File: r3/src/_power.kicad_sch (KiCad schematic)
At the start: 51 parts, among them J10 Conn_01x05_MountingPin, Q1 Si7113ADN, Q2 Si7113ADN, Q3 Si7113ADN, U2 ESD7004, U3 DZDH0401DW, U4 DZDH0401DW, U5 LM60440DRPK, U6 LM60440DRPK

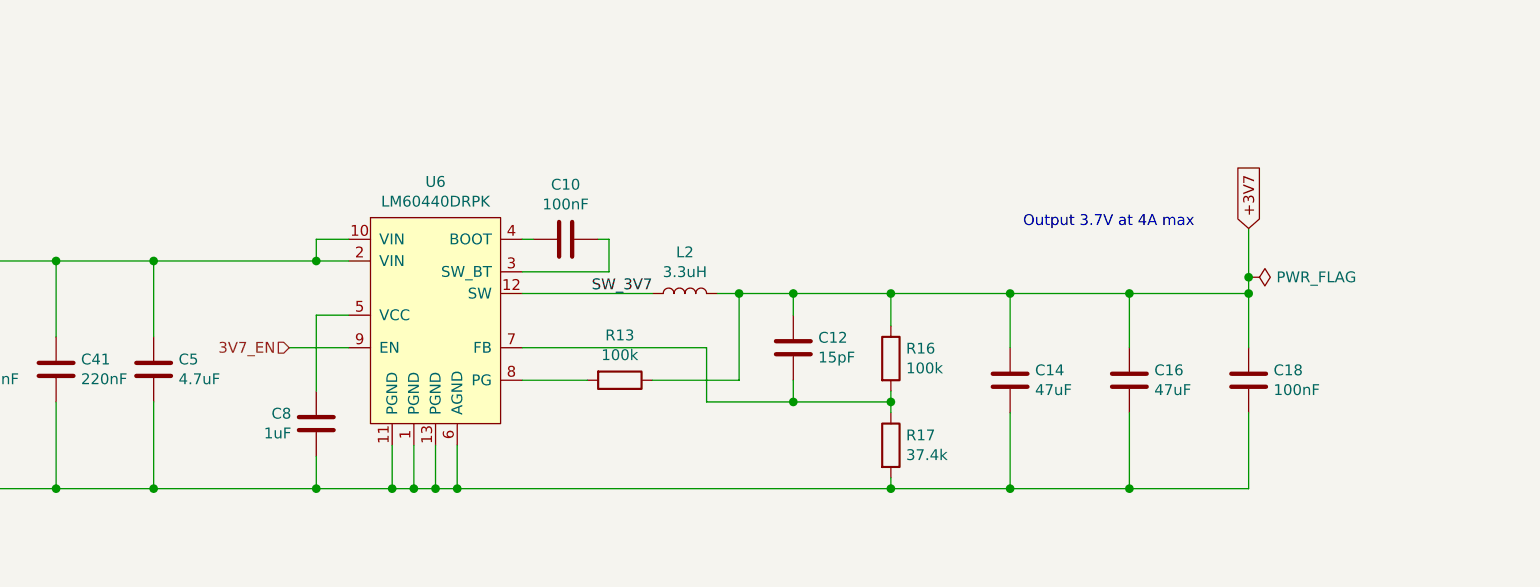
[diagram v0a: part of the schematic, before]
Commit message: Add pull-down on 3V7_EN
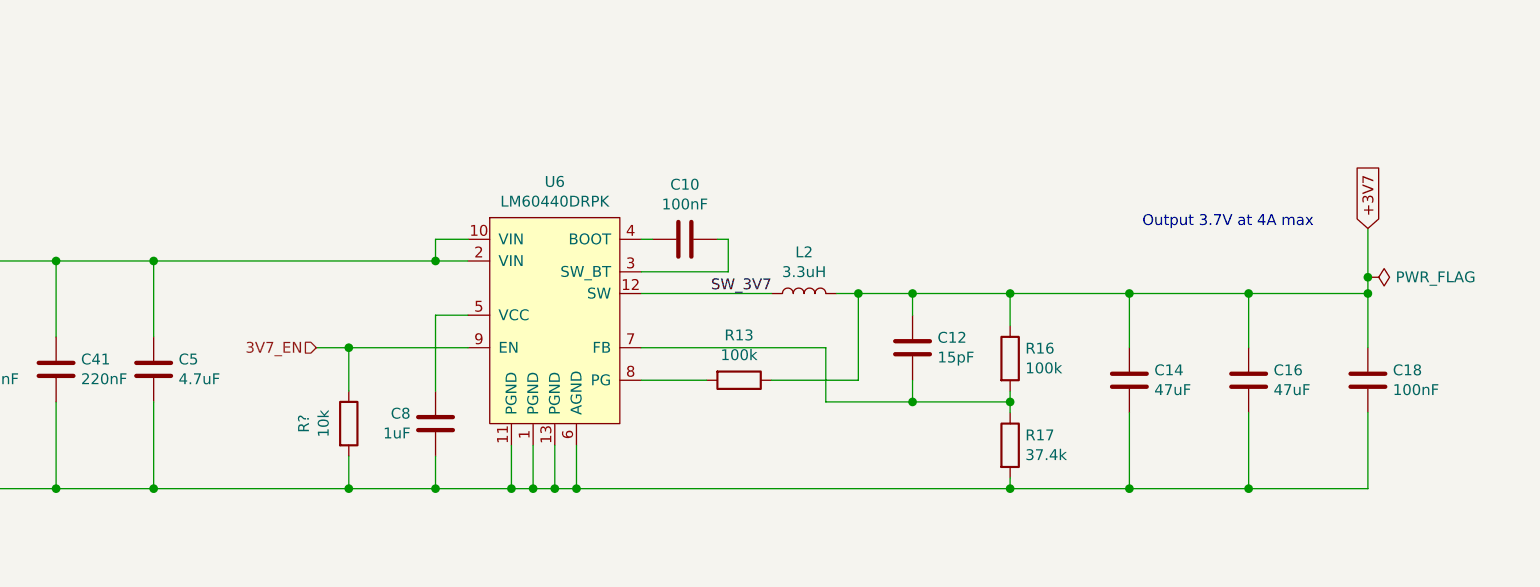
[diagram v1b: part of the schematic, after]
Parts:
- added R?: 10k, Resistor_SMD:R_0603_1608Metric, symbol Device:R
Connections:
- net 3V7_EN: now also R?.1
- net GND: now also R?.2
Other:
- moved on the sheet: C10, C12, C14, C16, C18, C8, L2, R13, R16, R17, U6

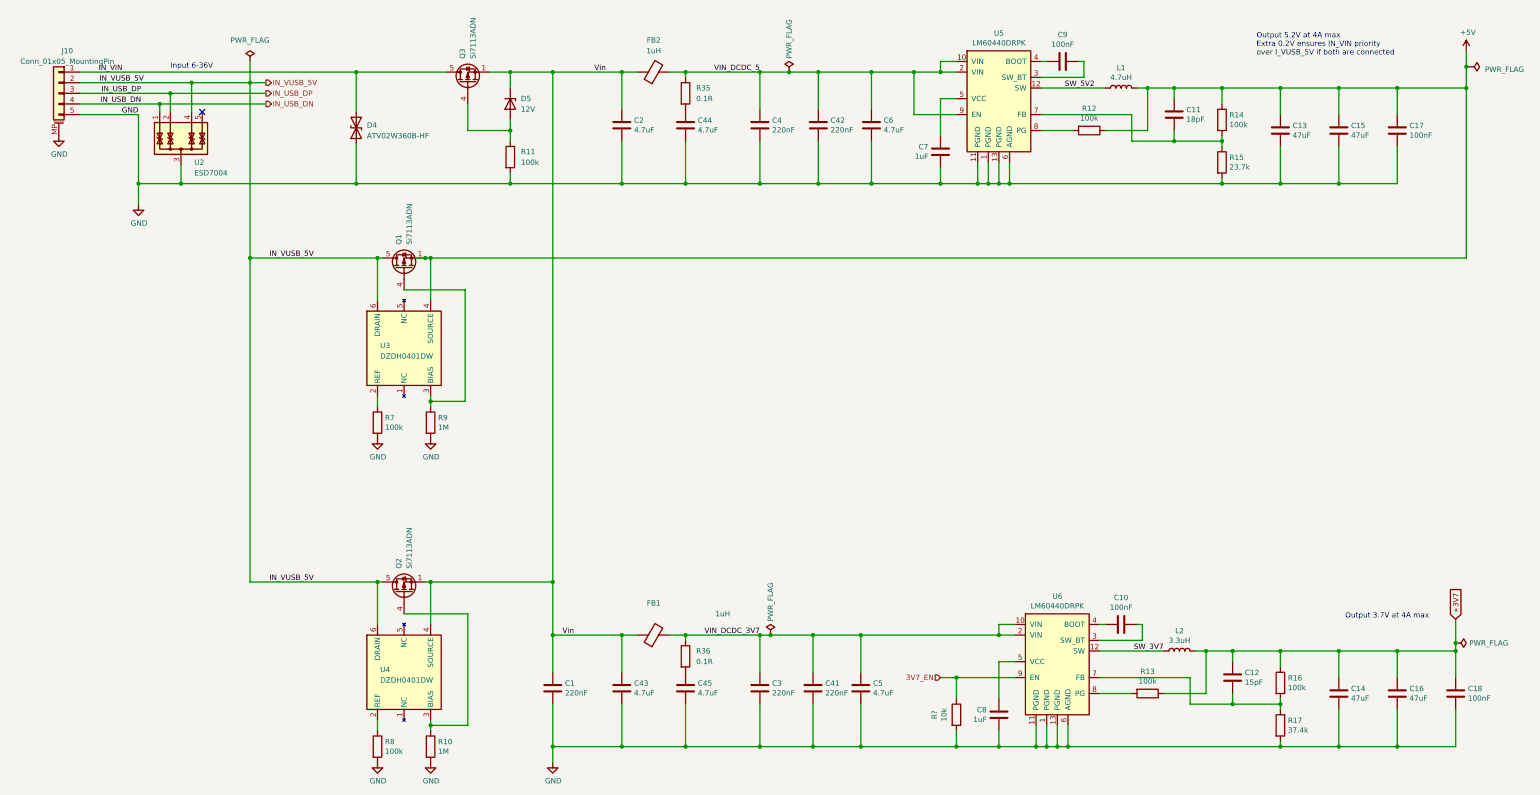
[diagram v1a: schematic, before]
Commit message: Change to Molex CLIK-Mate for input connector
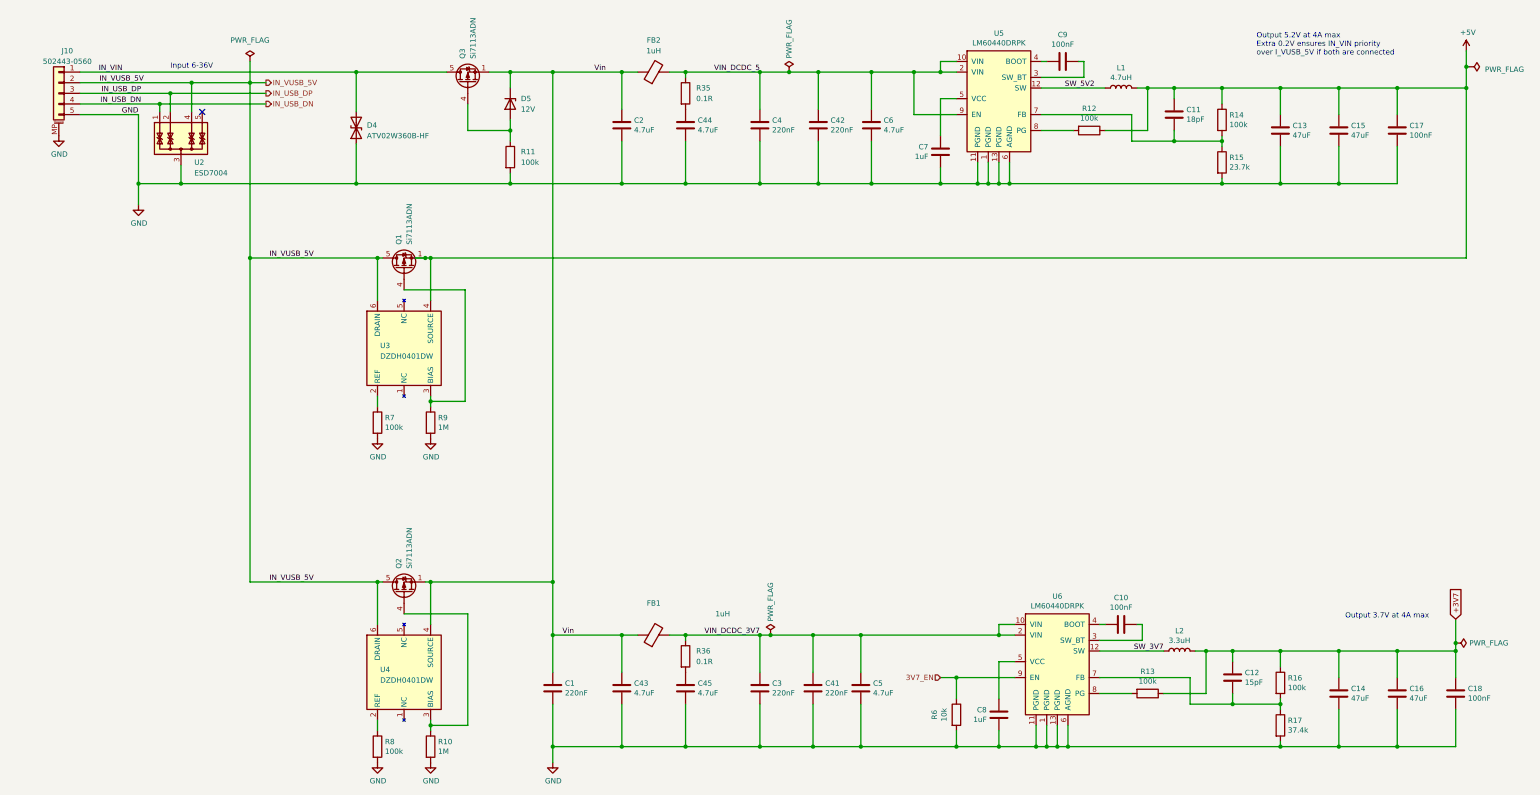
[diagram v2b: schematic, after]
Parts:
- J10: value Conn_01x05_MountingPin -> 502443-0560; footprint Connector_JST:JST_PH_B5B-PH-SM4-TB_1x05-1MP_P2.00mm_Vertical -> Connector_Molex:Molex_CLIK-Mate_502443-0570_1x05-1MP_P2.00mm_Vertical
- gave numbers to parts that had none: 1
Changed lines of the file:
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@@
   (symbol (lib_id "Device:R") (at 264.16 220.98 0) (unit 1)
     (in_bom yes) (on_board yes)
-    (property "Reference" "R?" (id 0) (at 258.9022 220.98 90))
+    (property "Reference" "R6" (id 0) (at 258.9022 220.98 90))
     (property "Value" "10k" (id 1) (at 261.2136 220.98 90))
     (property "Footprint" "Resistor_SMD:R_0603_1608Metric" (id 2) (at 262.382 220.98 90)
@@
     (in_bom yes) (on_board yes)
     (property "Reference" "J10" (id 0) (at 51.562 62.23 0))
-    (property "Value" "Conn_01x05_MountingPin" (id 1) (at 51.562 64.77 0))
-    (property "Footprint" "Connector_JST:JST_PH_B5B-PH-SM4-TB_1x05-1MP_P2.00mm_Vertical" (id 2) (at 49.53 72.39 0)
-      (effects (font (size 1.27 1.27)) hide)
-    )
+    (property "Value" "502443-0560" (id 1) (at 51.562 64.77 0))
+    (property "Footprint" "Connector_Molex:Molex_CLIK-Mate_502443-0570_1x05-1MP_P2.00mm_Vertical" (id 2) (at 49.53 72.39 0)
+      (effects (font (size 1.27 1.27)) hide)
+    )

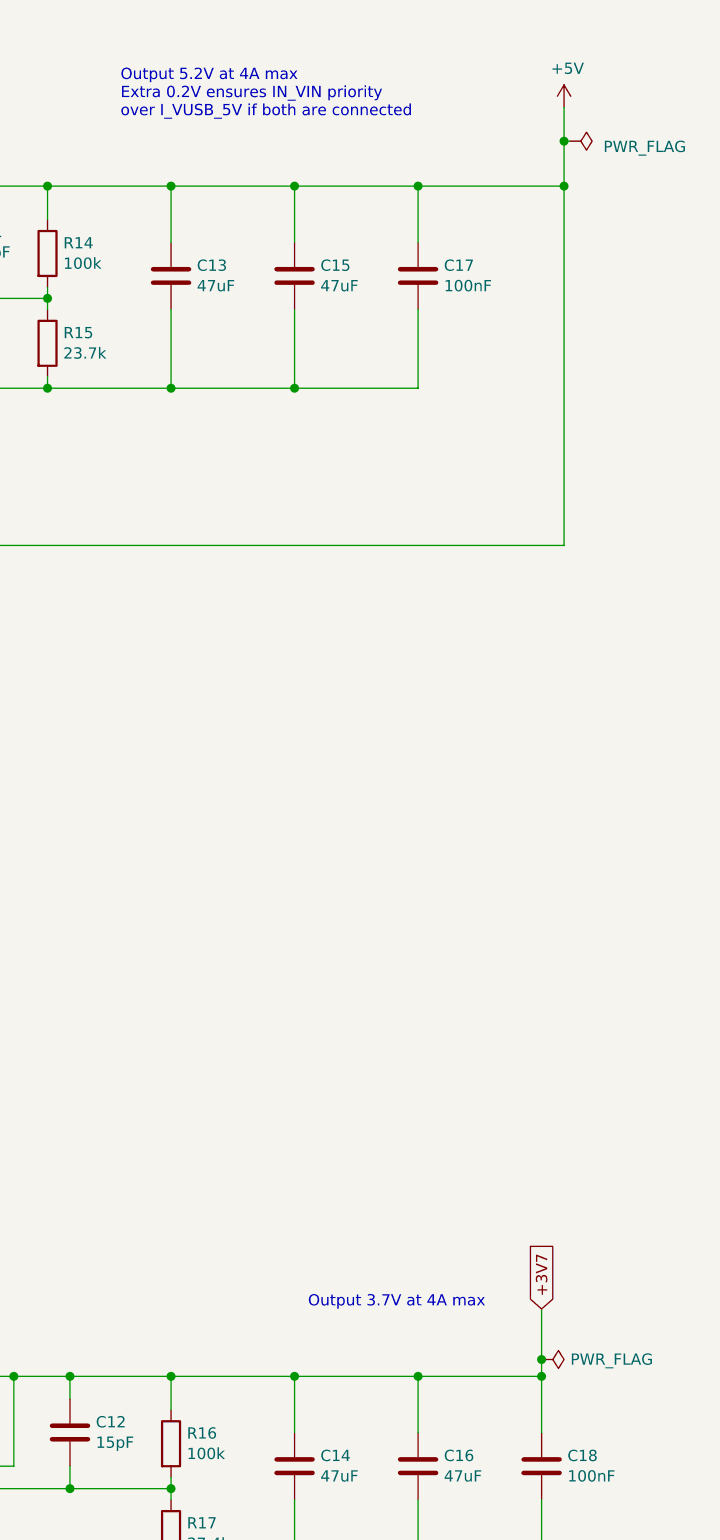
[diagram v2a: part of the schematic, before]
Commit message: Add 5V and 3V7 test points
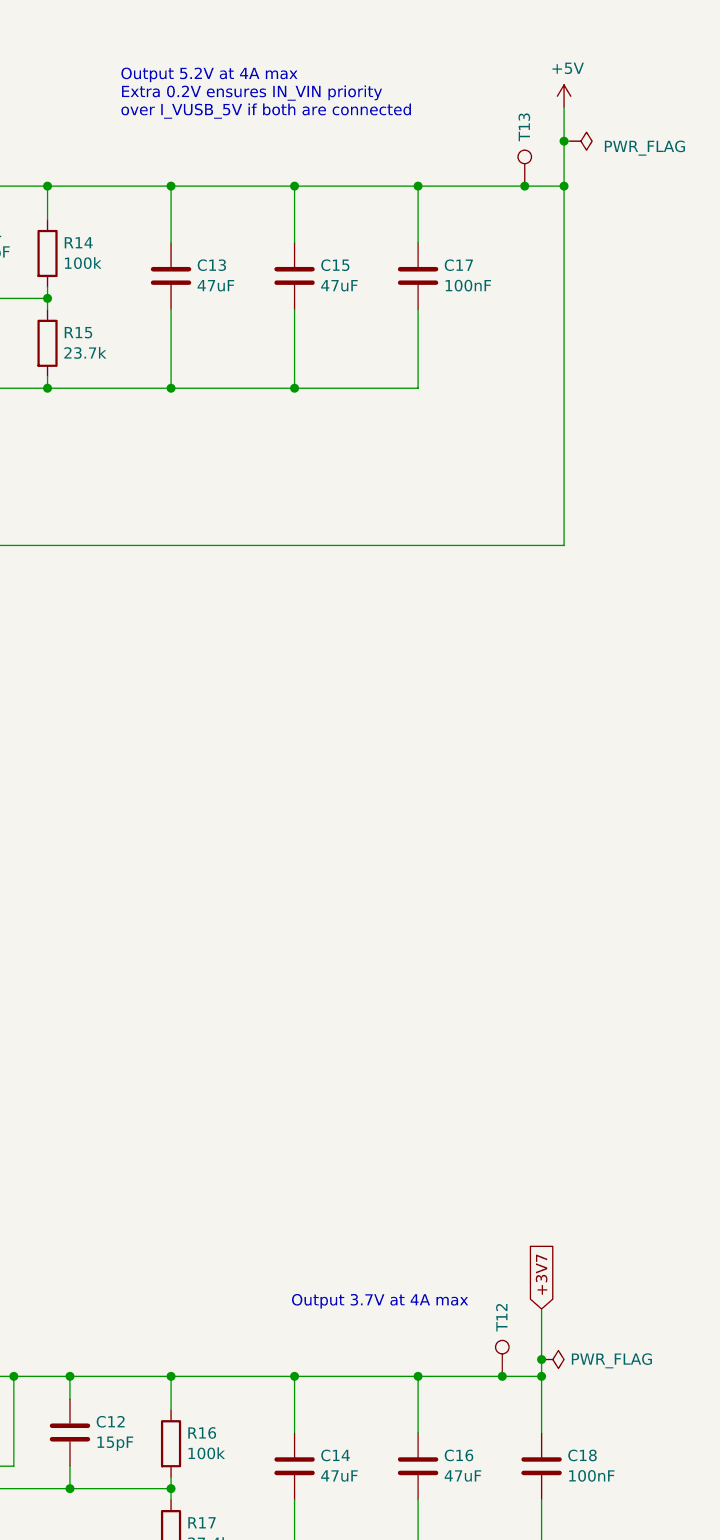
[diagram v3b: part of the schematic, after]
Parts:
- added T12, T13: (no value), TestPoint:TestPoint_Pad_D1.0mm, symbol Connector:TestPoint
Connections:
- net +3V7: now also T12.1
- net +5V: now also T13.1
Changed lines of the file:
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@@
   (junction (at 369.57 205.74) (diameter 1.016) (color 0 0 0 0))
   (junction (at 369.57 228.6) (diameter 1.016) (color 0 0 0 0))
+  (junction (at 379.095 205.74) (diameter 1.016) (color 0 0 0 0))
+  (junction (at 381.635 71.12) (diameter 1.016) (color 0 0 0 0))
   (junction (at 383.54 203.835) (diameter 1.016) (color 0 0 0 0))
   (junction (at 383.54 205.74) (diameter 1.016) (color 0 0 0 0))
@@
     (stroke (width 0) (type solid) (color 0 0 0 0))
   )
-  (wire (pts (xy 369.57 71.12) (xy 386.08 71.12))
+  (wire (pts (xy 369.57 71.12) (xy 381.635 71.12))
     (stroke (width 0) (type solid) (color 0 0 0 0))
   )
@@
     (stroke (width 0) (type solid) (color 0 0 0 0))
   )
-  (wire (pts (xy 369.57 205.74) (xy 383.54 205.74))
+  (wire (pts (xy 369.57 205.74) (xy 379.095 205.74))
     (stroke (width 0) (type solid) (color 0 0 0 0))
   )
   (wire (pts (xy 369.57 219.71) (xy 369.57 228.6))
+    (stroke (width 0) (type solid) (color 0 0 0 0))
+  )
+  (wire (pts (xy 379.095 205.74) (xy 383.54 205.74))
+    (stroke (width 0) (type solid) (color 0 0 0 0))
+  )
+  (wire (pts (xy 381.635 71.12) (xy 386.08 71.12))
     (stroke (width 0) (type solid) (color 0 0 0 0))
   )
@@
     (effects (font (size 1.27 1.27)) (justify left bottom))
   )
-  (text "Output 3.7V at 4A max" (at 377.19 198.12 180)
+  (text "Output 3.7V at 4A max" (at 375.285 198.12 180)
     (effects (font (size 1.27 1.27)) (justify right bottom))
   )
@@
       (effects (font (size 1.27 1.27)) hide)
     )
+    (pin "1")
+  )
+  (symbol (lib_id "Connector:TestPoint") (at 379.095 205.74 0) (unit 1)
+    (in_bom yes) (on_board yes)
+    (property "Reference" "T12" (id 0) (at 379.095 200.66 90)
+      (effects (font (size 1.27 1.27)) (justify left))
+    )
+    (property "Value" " " (id 1) (at 377.825 200.66 90)
+      (effects (font (size 1.27 1.27)) (justify left))
+    )
+    (property "Footprint" "TestPoint:TestPoint_Pad_D1.0mm" (id 2) (at 384.175 205.74 0)
+      (effects (font (size 1.27 1.27)) hide)
+    )
+    (property "Datasheet" "~" (id 3) (at 384.175 205.74 0)
+      (effects (font (size 1.27 1.27)) hide)
+    )
+    (pin "1")
+  )
+  (symbol (lib_id "Connector:TestPoint") (at 381.635 71.12 0) (unit 1)
+    (in_bom yes) (on_board yes)
+    (property "Reference" "T13" (id 0) (at 381.635 66.04 90)
+      (effects (font (size 1.27 1.27)) (justify left))
+    )
+    (property "Value" " " (id 1) (at 380.365 66.04 90)
+      (effects (font (size 1.27 1.27)) (justify left))
+    )
+    (property "Footprint" "TestPoint:TestPoint_Pad_D1.0mm" (id 2) (at 386.715 71.12 0)
+      (effects (font (size 1.27 1.27)) hide)
+    )
+    (property "Datasheet" "~" (id 3) (at 386.715 71.12 0)
+      (effects (font (size 1.27 1.27)) hide)
+    )

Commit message: Change to new 5-pin variant of the protection diode network symbol
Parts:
- U2: footprint jeffmakes-footprints:USON-10_2.5x1.0mm_P0.5mm -> Package_SON:USON-10_2.5x1.0mm_P0.5mm; symbol Power_Protection:TPD4E02B04DQA -> j_Power_Protection:ESD7004
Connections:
- net GND: no longer U2.8 (G)
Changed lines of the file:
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@@
     (pin "MP")
   )
-  (symbol (lib_id "Power_Protection:TPD4E02B04DQA") (at 78.74 84.455 0) (unit 1)
+  (symbol (lib_id "j_Power_Protection:ESD7004") (at 78.74 84.455 0) (unit 1)
     (in_bom yes) (on_board yes)
     (property "Reference" "U2" (id 0) (at 81.915 88.9 0)
@@
       (effects (font (size 1.27 1.27)) (justify left))
     )
-    (property "Footprint" "jeffmakes-footprints:USON-10_2.5x1.0mm_P0.5mm" (id 2) (at 86.36 84.455 0)
+    (property "Footprint" "Package_SON:USON-10_2.5x1.0mm_P0.5mm" (id 2) (at 86.36 84.455 0)
       (effects (font (size 1.27 1.27)) (justify left) hide)
     )
@@
     (pin "3")
     (pin "1")
-    (pin "10")
     (pin "2")
     (pin "4")
     (pin "5")
-    (pin "6")
-    (pin "7")
-    (pin "8")
-    (pin "9")
   )
   (symbol (lib_id "j_Power_Management:DZDH0401DW") (at 133.35 132.08 0) (unit 1)

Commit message: Change all diode protection networks to a 5-pin variant to prevent DRC errors due to missing pads
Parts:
- U2: footprint Package_SON:USON-10_2.5x1.0mm_P0.5mm -> jeffmakes-footprints:USON-10_2.5x1.0mm_P0.5mm
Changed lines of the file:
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@@
       (effects (font (size 1.27 1.27)) (justify left))
     )
-    (property "Footprint" "Package_SON:USON-10_2.5x1.0mm_P0.5mm" (id 2) (at 86.36 84.455 0)
+    (property "Footprint" "jeffmakes-footprints:USON-10_2.5x1.0mm_P0.5mm" (id 2) (at 86.36 84.455 0)
       (effects (font (size 1.27 1.27)) (justify left) hide)
     )
